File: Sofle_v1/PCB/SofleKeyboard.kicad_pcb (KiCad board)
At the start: 2 copper layers, 156 x 109.2 mm, 98 parts, among them J1 LED, J2 4PIN, J3 OLED, P1 i2c_pin, P2 i2c_pin, SW1 SW_PUSH, SW10 SW_PUSH, SW11 SW_PUSH, SW12 SW_PUSH, SW13 SW_PUSH, SW14 SW_PUSH, SW15 SW_PUSH, SW16 SW_PUSH, SW17 SW_PUSH, SW18 SW_PUSH, SW19 SW_PUSH, SW2 SW_PUSH, SW20 SW_PUSH, SW21 SW_PUSH, SW22 SW_PUSH, SW23 SW_PUSH, SW24 SW_PUSH, SW25 Rotary_Encoder_Switch, SW26 SW_PUSH, SW27 SW_PUSH, SW28 SW_PUSH, SW29 SW_PUSH, SW3 SW_PUSH, SW30 SW_PUSH, SW31 SW_PUSH, SW32 SW_PUSH, SW33 SW_PUSH, SW34 SW_PUSH, SW35 SW_PUSH, SW4 SW_PUSH, SW5 SW_PUSH, SW6 SW_PUSH, SW7 SW_PUSH, SW8 SW_PUSH, SW9 SW_PUSH, U1 ProMicro

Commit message: Cleanup
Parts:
- SW35: footprint SofleKeyboard-footprint:CherryMX_KailhLowProfile_Hotswap -> SofleKeyboard-footprint:CherryMX_KailhLowProfile_Hotswap_1.5
- moved D7 9.10 mm to (123.5, 61.1)
- moved D1 2.58 mm to (116.5, 59.5)
- moved JP2 2.30 mm to (101.8, 71.6)
- moved JP6 2.30 mm to (101.8, 71.6)
- moved JP1 2.30 mm to (104.3, 71.6)
- moved JP3 2.30 mm to (99.2, 71.6)
- moved JP4 2.30 mm to (96.7, 71.6)
- moved JP5 2.30 mm to (104.3, 71.6)
- moved JP7 2.30 mm to (99.2, 71.6)
- moved JP8 2.30 mm to (96.7, 71.6)
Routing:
- net GND: track 124.4 -> 40.3 mm, vias 44 -> 43
- net Net-(D7-A): track 37.3 -> 28.6 mm
- net Net-(J3-P4): track 9.62 -> 5.02 mm
- net Net-(J3-P2): track 9.63 -> 5.03 mm
- net Net-(J3-P1): track 9.60 -> 5.00 mm
- net Net-(J3-P3): track 9.67 -> 5.15 mm
- net SDA: track 57.0 -> 60.8 mm
- net VCC: track 74.2 -> 77.0 mm
- net row1: track 165.1 -> 167.0 mm
- net Net-(D1-A): track 27.9 -> 28.9 mm
- net SCL: track 50.1 -> 51.0 mm
- net row0: track 161.4 -> 160.7 mm, vias 2 -> 3
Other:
- board text added: "C0"
- board text added: "C1"
- board text added: "C2"
- board text added: "C3"
- board text added: "C4"
- board text added: "C5"
- board text added: "C6"
- board text added: "DATA"
- board text added: "ENCA"
- board text added: "ENCB"
- board text added: "GND"
- board text added: "LED"
- board text added: "R0"
- board text added: "R1"
- board text added: "R2"
- board text added: "R3"
- board text added: "R4"
- board text added: "RESET"
- board text added: "SCL"
- board text added: "SDA"
- board text added: "VCC"

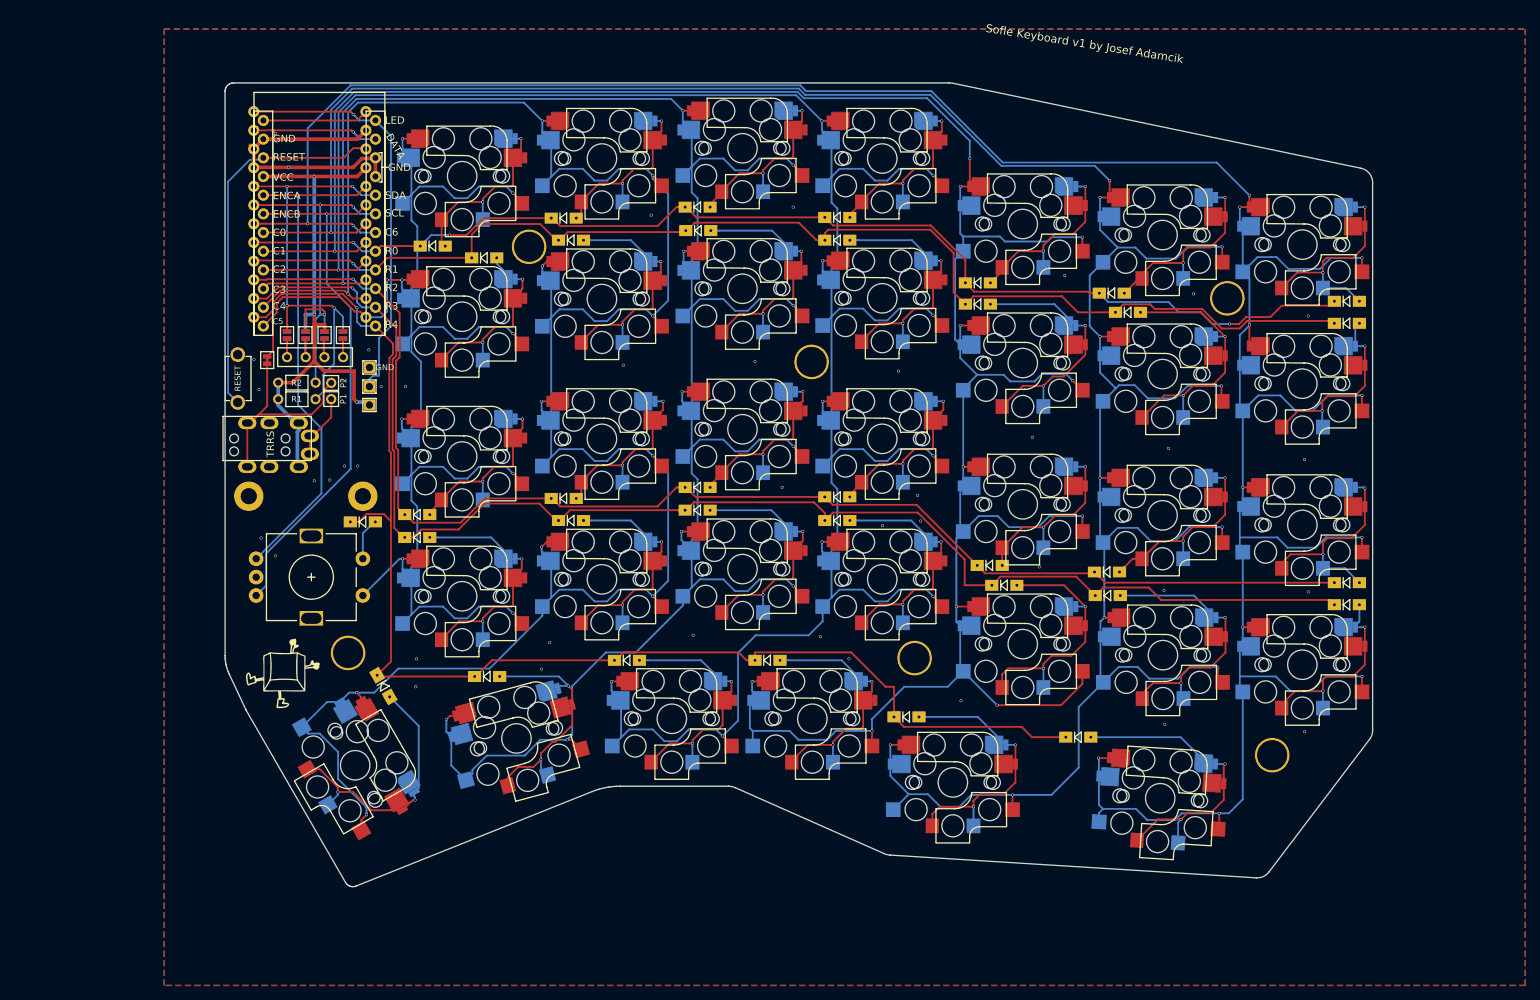
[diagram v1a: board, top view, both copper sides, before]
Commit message: Moved TRRS + battery connector.
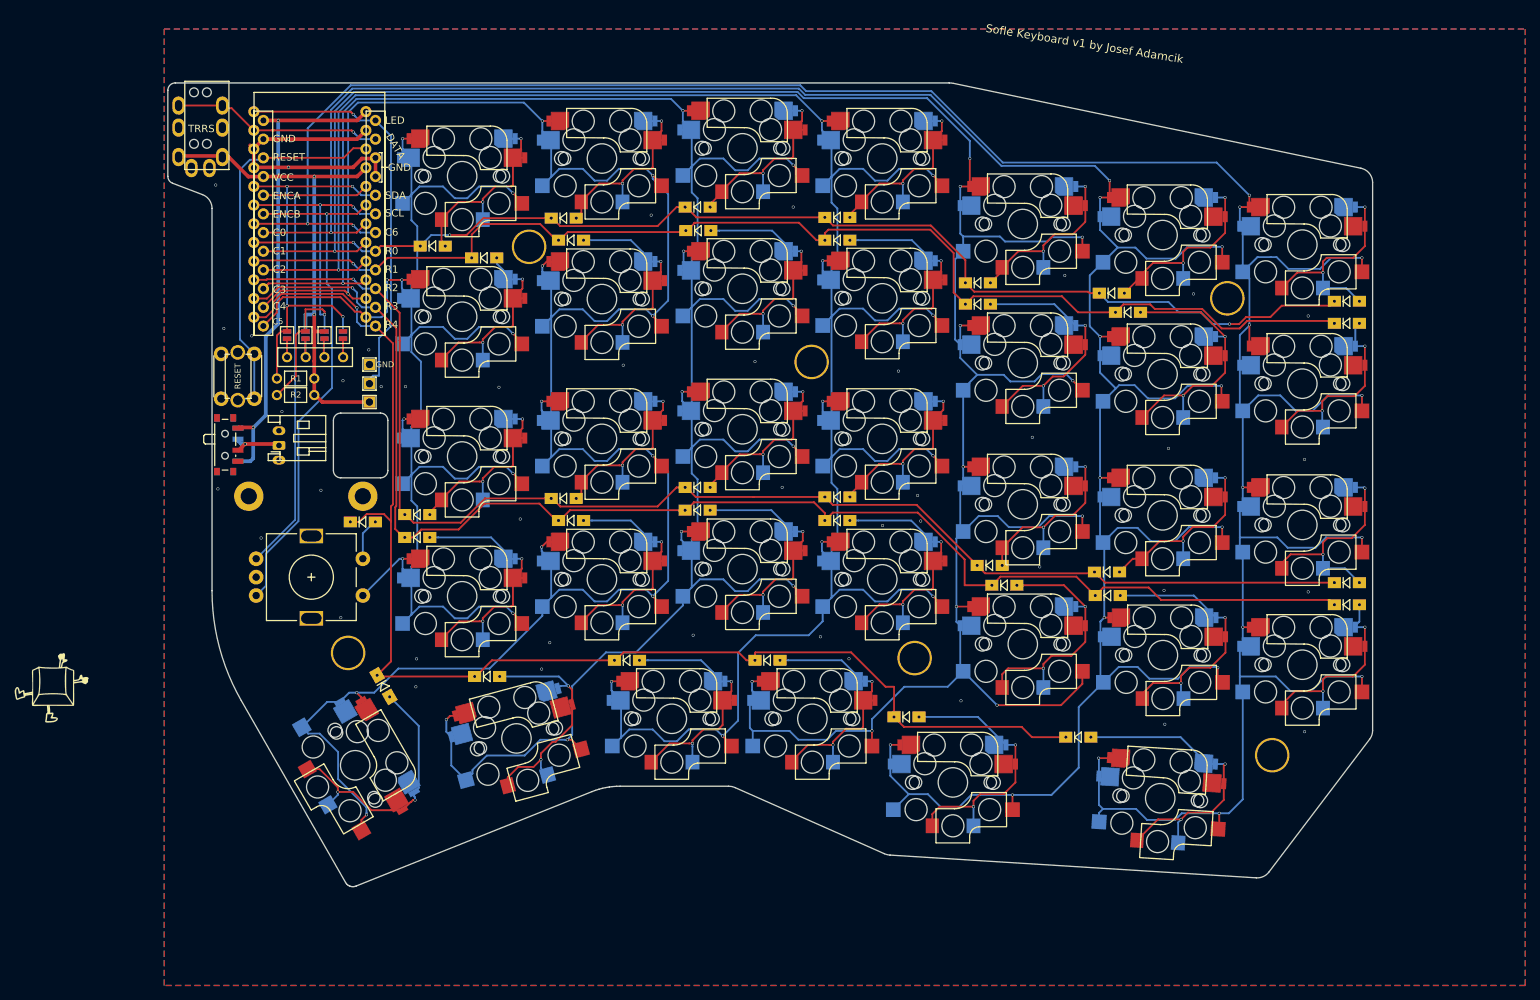
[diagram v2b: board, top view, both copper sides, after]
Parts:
- removed P1, P2: i2c_pin, SofleKeyboard-footprint:1pin_conn
- removed W1: jumper, SofleKeyboard-footprint:jumper_data
- added BATT_HIGH1: BATT_GND, SofleKeyboard-footprint:Sofle_JST_PH_S2B-PH-K_1x02_P2.00mm_Horizontal, F.Cu at (95.6, 86.6)
- added SW_POW1: POWER_SWITCH, SofleKeyboard-footprint:Sofle_SW_SPDT_PCM12, F.Cu at (88.6, 86.5)
- RSW1: footprint SofleKeyboard-footprint:TACT_SWITCH_TVBP06 -> SofleKeyboard-footprint:Sofle_Tactile Switch
- SW35: footprint SofleKeyboard-footprint:CherryMX_KailhLowProfile_Hotswap_1.5 -> SofleKeyboard-footprint:CherryMX_KailhLowProfile_Hotswap
- moved J2 48.6 mm to (85.8, 37.1), turned to 0 degrees
- moved Ref** 31.5 mm to (64.4, 126.5)
- moved Ref** 31.5 mm to (65.3, 126.6)
- moved R1 2.82 mm to (97.9, 77.5), turned to 180 degrees
- moved R2 1.70 mm to (97.9, 79.8), turned to 180 degrees
- moved J1 0.40 mm to (107.9, 80.7)
- moved RSW1 0.30 mm to (90.0, 77.2)
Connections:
- J2 pad 3: /i2c_d -> DATA
- J2 pad 4: /i2c_c -> unconnected-(J2-Pad4)
- U1 pad 24: unconnected-(U1-RAW-Pad24) -> B_RAW
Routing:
- net B_RAW: track 0.00 -> 66.1 mm, vias 0 -> 2
- net /i2c_d: track 29.6 -> 0.00 mm
- net DATA: track 48.9 -> 29.0 mm, vias 3 -> 1
- net (no net): track 14.4 -> 0.00 mm
- net /i2c_c: track 9.85 -> 0.00 mm
- net /BATT_HIGH: track 0.00 -> 7.36 mm, vias 0 -> 1
- net VCC: track 77.0 -> 69.8 mm, vias 3 -> 2
- net SDA: track 60.8 -> 54.7 mm
- net ENCA: track 68.8 -> 66.0 mm
- net ENCB: track 73.0 -> 70.9 mm
- net RESET: track 51.2 -> 52.7 mm
- net SCL: track 51.0 -> 52.2 mm
- net GND: track 40.3 -> 39.6 mm, vias 43 -> 44
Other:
- board size 156 x 109.2 mm -> 163.8 x 109.2 mm

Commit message: Plates.
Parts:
- moved Ref** 31.5 mm to (96.8, 125.4)
- moved Ref** 31.5 mm to (95.9, 125.4)
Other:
- board text added: "Sofle 70 by Davide Stasio"
- board text added: "col0"
- board text added: "col1"
- board text added: "col2"
- board text added: "col3"
- board text added: "col4"
- board text added: "col5"
- board text added: "col6"
- board text added: "r1"
- board text added: "r2"
- board text added: "row0"
- board text added: "row1"
- board text added: "row2"
- board text added: "row3"
- board text added: "row4"
- board text removed: "C0"
- board text removed: "C1"
- board text removed: "C2"
- board text removed: "C3"
- board text removed: "C4"
- board text removed: "C5"
- board text removed: "C6"
- board text removed: "R0"
- board text removed: "R1"
- board text removed: "R2"
- board text removed: "R3"
- board text removed: "R4"
- board text removed: "Sofle Keyboard v1 by Josef Adamcik"

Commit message: Bugfixes.
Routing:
- net GND: track 39.6 -> 45.0 mm, vias 44 -> 45
- net col5: track 205.8 -> 204.2 mm
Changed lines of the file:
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@@
 	)
 	(segment
+		(start 92.4 72.2)
+		(end 91.9 71.7)
+		(width 0.5)
+		(layer "F.Cu")
+		(net 34)
+	)
+	(segment
 		(start 93.478815 44.965745)
 		(end 96.9 44.965745)
@@
 		(net 34)
 	)
+	(segment
+		(start 94.501 72.2)
+		(end 92.4 72.2)
+		(width 0.5)
+		(layer "F.Cu")
+		(net 34)
+	)
 	(via
 		(at 202.4 63.5)
@@
 	)
 	(via
+		(at 94.501 72.2)
+		(size 0.4)
+		(drill 0.3)
+		(layers "F.Cu" "B.Cu")
+		(net 34)
+	)
+	(via
 		(at 96.9 44.965745)
 		(size 0.4)
@@
 	)
 	(segment
+		(start 96.10038 71.09962)
+		(end 95 72.2)
+		(width 0.5)
+		(layer "B.Cu")
+		(net 34)
+	)
+	(segment
+		(start 96.7 71.09962)
+		(end 96.10038 71.09962)
+		(width 0.5)
+		(layer "B.Cu")
+		(net 34)
+	)
+	(segment
+		(start 95 72.2)
+		(end 94.501 72.2)
+		(width 0.5)
+		(layer "B.Cu")
+		(net 34)
+	)
+	(segment
 		(start 106.17 57.67)
 		(end 107.47 56.37)
@@
 	)
 	(segment
-		(start 114.9 75.2)
-		(end 114.9 82.76)
-		(width 0.25)
-		(layer "B.Cu")
-		(net 51)
-	)
-	(segment
 		(start 113.56 47.5)
 		(end 113.6 47.46)
@@
 	)
 	(segment
-		(start 113.6 56)
-		(end 114.4 56.8)
-		(width 0.25)
-		(layer "B.Cu")
-		(net 51)
-	)
-	(segment
 		(start 113.6 103.06)
 		(end 113.6 104.56)
@@
 	)
 	(segment
-		(start 113.6 64.5)
-		(end 114.4 63.7)
+		(start 113.4 64.3)
+		(end 113.6 64.5)
 		(width 0.25)
 		(layer "B.Cu")
@@
 	)
 	(segment
-		(start 112 66.6)
-		(end 113.56 66.6)
+		(start 113.4 56.2)
+		(end 113.4 64.3)
 		(width 0.25)
 		(layer "B.Cu")
@@
 	)
 	(segment
-		(start 113.6 52.5)
-		(end 113.6 56)
+		(start 112 66.6)
+		(end 113.56 66.6)
 		(width 0.25)
 		(layer "B.Cu")
@@
 	)
 	(segment
-		(start 113.6 64.5)
-		(end 113.6 66.56)
+		(start 113.6 56)
+		(end 113.4 56.2)
 		(width 0.25)
 		(layer "B.Cu")
@@
 	)
 	(segment
-		(start 113.56 104.6)
-		(end 113.6 104.56)
+		(start 113.6 71.6)
+		(end 113.6 85.56)
 		(width 0.25)
 		(layer "B.Cu")
@@
 	)
 	(segment
-		(start 114.9 82.76)
-		(end 113.6 84.06)
+		(start 113.56 104.6)
+		(end 113.6 104.56)
 		(width 0.25)
 		(layer "B.Cu")
@@
 	)
 	(segment
+		(start 113.6 64.5)
+		(end 113.6 66.56)
+		(width 0.25)
+		(layer "B.Cu")
+		(net 51)
+	)
+	(segment
 		(start 114.4 94.9)
 		(end 114.4 102.26)
@@
 	)
 	(segment
-		(start 114.4 56.8)
-		(end 114.4 63.7)
+		(start 113.6 52.5)
+		(end 113.6 56)
 		(width 0.25)
 		(layer "B.Cu")
@@
 	)
 	(segment
-		(start 113.6 73.9)
-		(end 114.9 75.2)
-		(width 0.25)
-		(layer "B.Cu")
-		(net 51)
-	)
-	(segment
-		(start 113.6 71.6)
-		(end 113.6 73.9)
-		(width 0.25)
-		(layer "B.Cu")
-		(net 51)
-	)
-	(segment
 		(start 117.9 51.4)
 		(end 119.5 53)
@@
 		(width 0.25)
 		(layer "B.Cu")
-		(net 51)
-	)
-	(segment
-		(start 113.6 84.06)
-		(end 113.6 85.56)
-		(width 0.25)
-		(layer "B.Cu")
